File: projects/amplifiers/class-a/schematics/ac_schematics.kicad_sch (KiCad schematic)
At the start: 11 parts, among them J1 5V, Q1 BC547

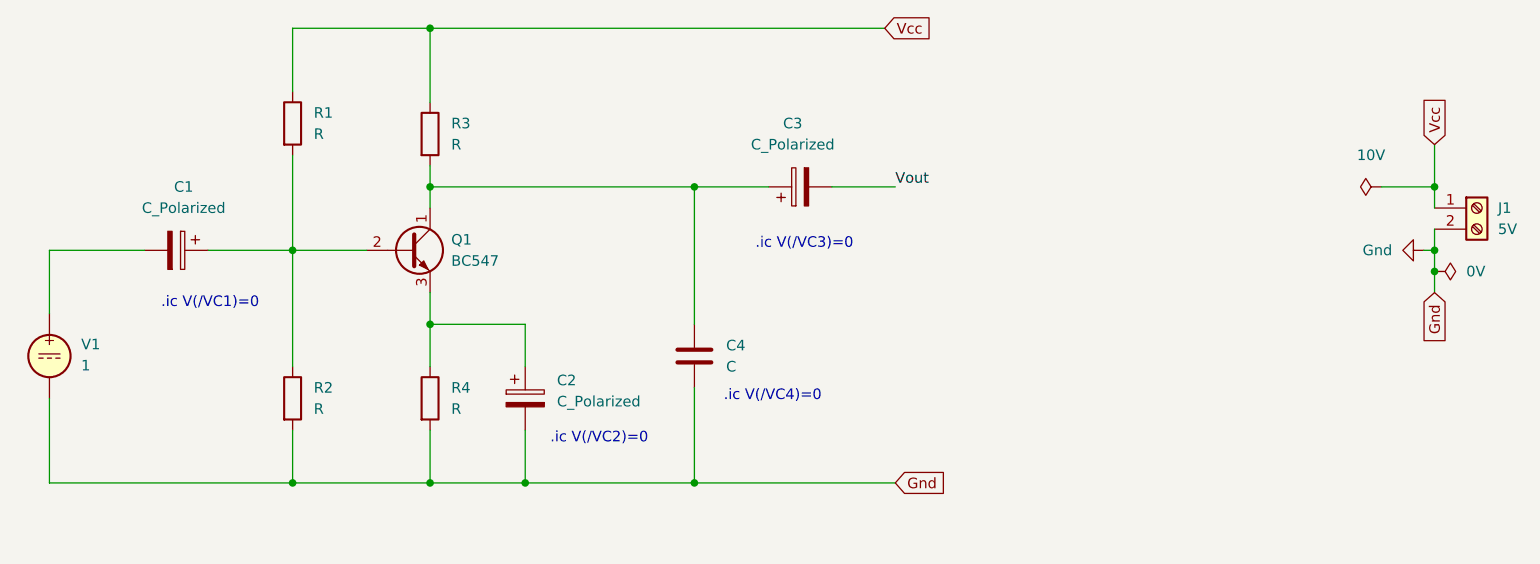
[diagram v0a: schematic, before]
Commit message: feat: Add AC analysis and simulations to Class-A amplifier
Adds AC circuit schematic with coupling/bypass capacitors
Includes AC simulation showing proper sine wave output
Document clipping behavior with excessive input amplitude
Update goals to separate DC and AC analysis tasks

Breaking changes: None

Resolves: None
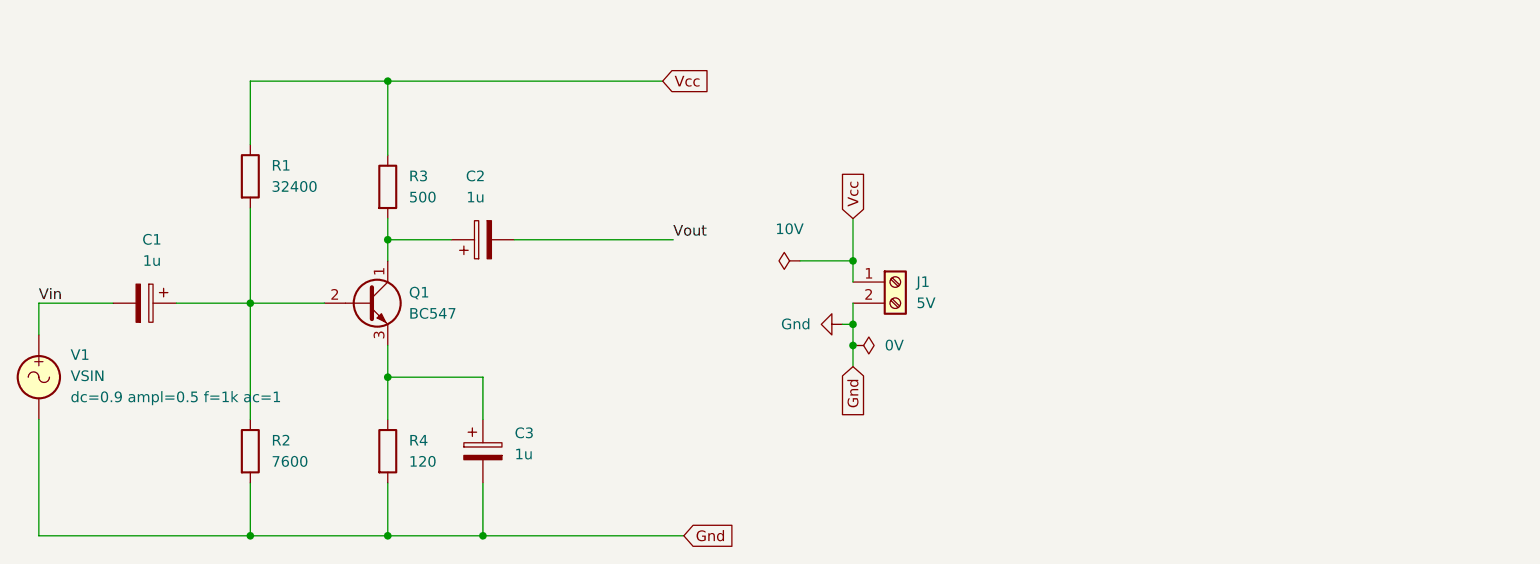
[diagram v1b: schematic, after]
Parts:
- removed C4: C, symbol Device:C
- removed V1: 1, symbol Simulation_SPICE:VDC
- added V1: VSIN, symbol Simulation_SPICE:VSIN
- C1, C2, C3: value C_Polarized -> 1u
- R1: value R -> 32400
- R2: value R -> 7600
- R3: value R -> 500
- R4: value R -> 120
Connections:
- net Gnd: now also C3.2, V1.2; no longer C2.2
- net Vout: now also C2.2; no longer C3.2
- net at Q1.3 (E), R4.1: now also C3.1; no longer C2.1
- net at Q1.1 (C), R3.2: now also C2.1; no longer C3.1
- net Vin: now reaches C1.2
- net Vin: now also V1.1
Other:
- note removed: ".ic V(/VC1)=0"
- note removed: ".ic V(/VC2)=0"
- note removed: ".ic V(/VC3)=0"
- note removed: ".ic V(/VC4)=0"
- moved on the sheet: J1

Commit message: feat: Updates class-A amplifier
Updates circuit schematics and simulation images for class-A amplifier
with new improved calculated capacitor values.

Breaking changes: None

Resolves: None
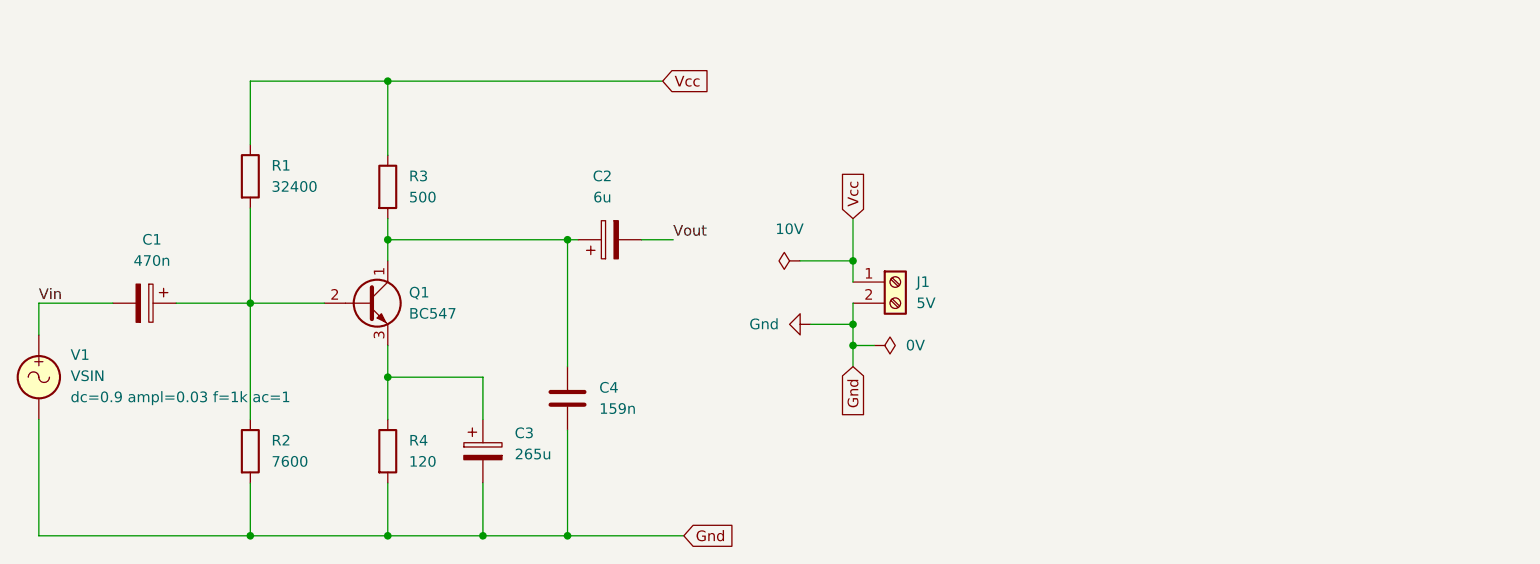
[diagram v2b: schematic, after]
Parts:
- added C4: 159n, symbol Device:C
- C1: value 1u -> 470n
- C2: value 1u -> 6u
- C3: value 1u -> 265u
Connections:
- net Gnd: now also C4.2
- net at C2.1, Q1.1 (C), R3.2: now also C4.1
